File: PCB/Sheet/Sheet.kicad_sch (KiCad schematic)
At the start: 17 parts, among them U1 MCP9700Ax-ELT, U2 MCP2562-E-MF, U3 ATtiny1616-M, U6 MCP2515-xST, Y1 8Hz

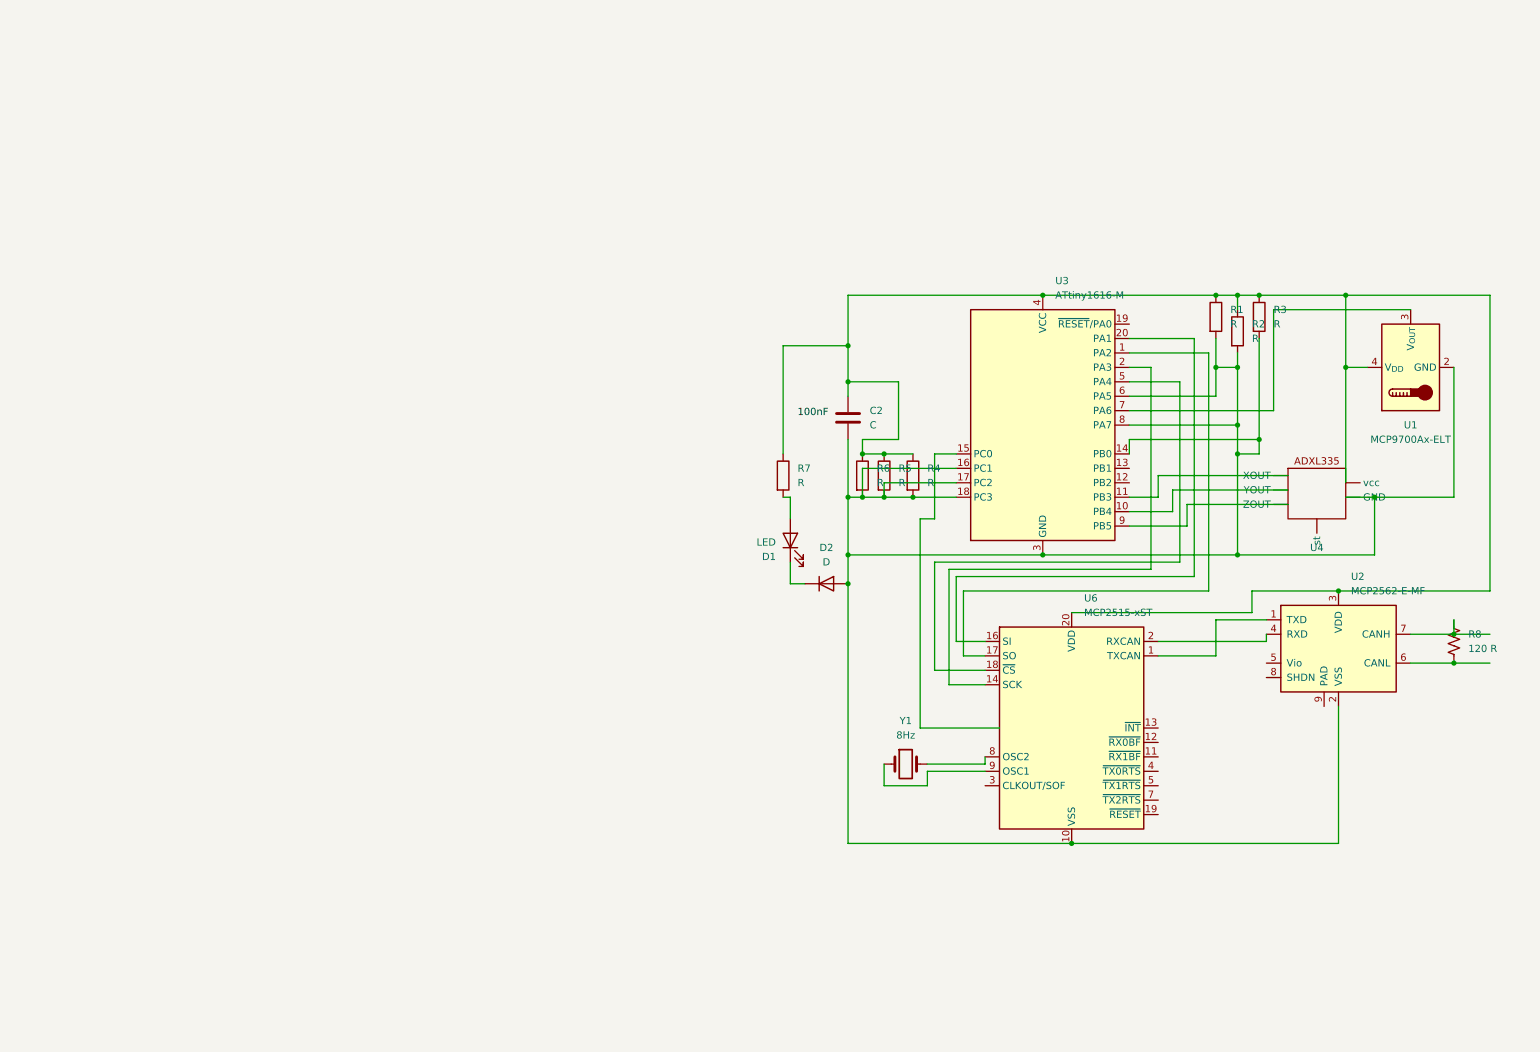
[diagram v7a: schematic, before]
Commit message: INtegration of multiplexer
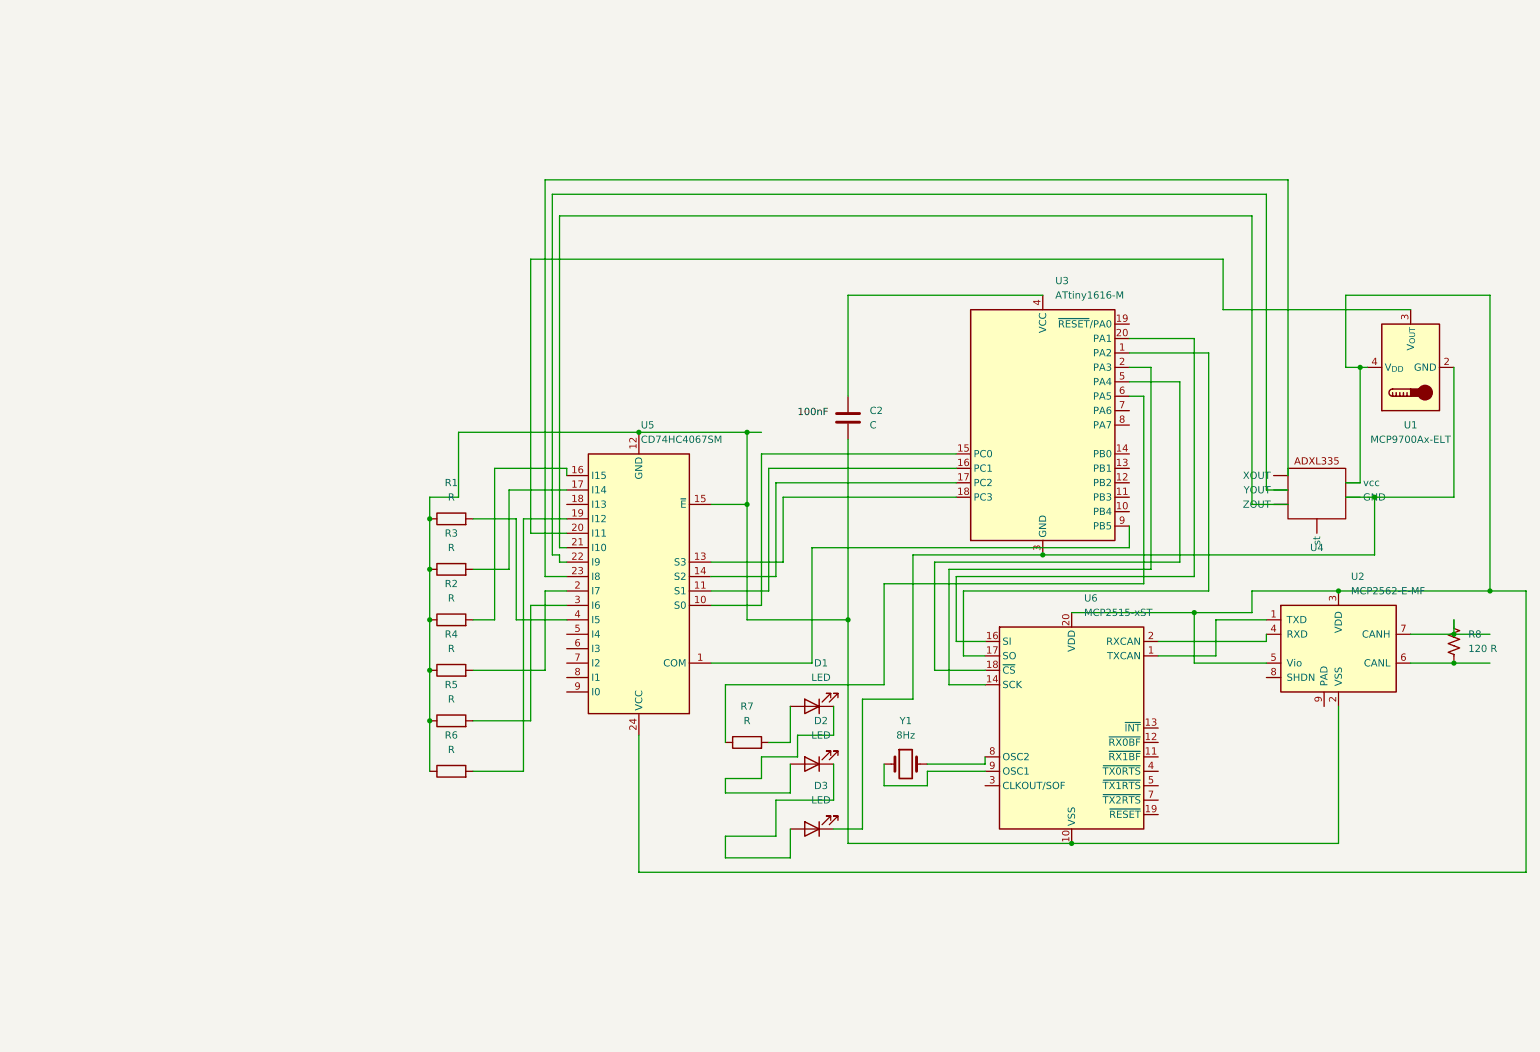
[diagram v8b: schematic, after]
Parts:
- removed D2: D, symbol Device:D
- added D2, D3: LED, symbol Device:LED
- added U5: CD74HC4067SM, Package_SO:SSOP-24_5.3x8.2mm_P0.65mm, symbol 74xx:CD74HC4067SM
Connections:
- net at U1.3 (V_{OUT}): now also U5.20 (I11); no longer U3.7 (PA6)
- net at U3.10 (PB4): no longer U4. (vcc)
- net at U3.11 (PB3): no longer U4. (vcc)
- net at U3.15 (PC0): now also U5.10 (S0); no longer U6.6 (NC)
- net at U3.9 (PB5): now also U5.1 (COM); no longer U4. (vcc)
- net at D1.1 (K): now also D2.2 (A)
- net at U2.5 (Vio): now also U1.4 (V_{DD}), U2.3 (VDD), U4. (vcc), U6.20 (VDD), U5.24 (VCC)
- new net: R7.1, U3.6 (PA5)
- new net: D3.1 (K), U1.2 (GND), U3.21 (GND), U3.3 (GND), U4. (vcc)
- new net: U3.16 (PC1), U5.11 (S1)
- new net: U3.17 (PC2), U5.14 (S2)
- new net: U3.18 (PC3), U5.13 (S3)
- new net: C2.1, U3.4 (VCC)
- new net: C2.2, R1.1, R2.1, R3.1, R4.1, R5.1, R6.1, U2.2 (VSS), U5.12 (GND), U5.15 (~{E}), U6.10 (VSS)
- new net: R2.2, U5.16 (I15)
- new net: R3.2, U5.17 (I14)
- new net: R6.2, U5.19 (I12)
- new net: R4.2, U5.2 (I7)
- new net: U4. (vcc), U5.21 (I10)
- new net: U4. (vcc), U5.22 (I9)
- new net: U4. (vcc), U5.23 (I8)
- new net: R5.2, U5.3 (I6)
- new net: R1.2, U5.4 (I5)
- new net: D2.1 (K), D3.2 (A)
- now unconnected: U3.14 (PB0), U3.8 (PA7), U4. (vcc), U4. (vcc)
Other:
- moved on the sheet: R1, R2, R3, R4, R5
